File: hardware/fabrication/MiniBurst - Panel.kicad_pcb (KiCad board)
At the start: 2 copper layers, 30 x 128.5 mm, 9 parts

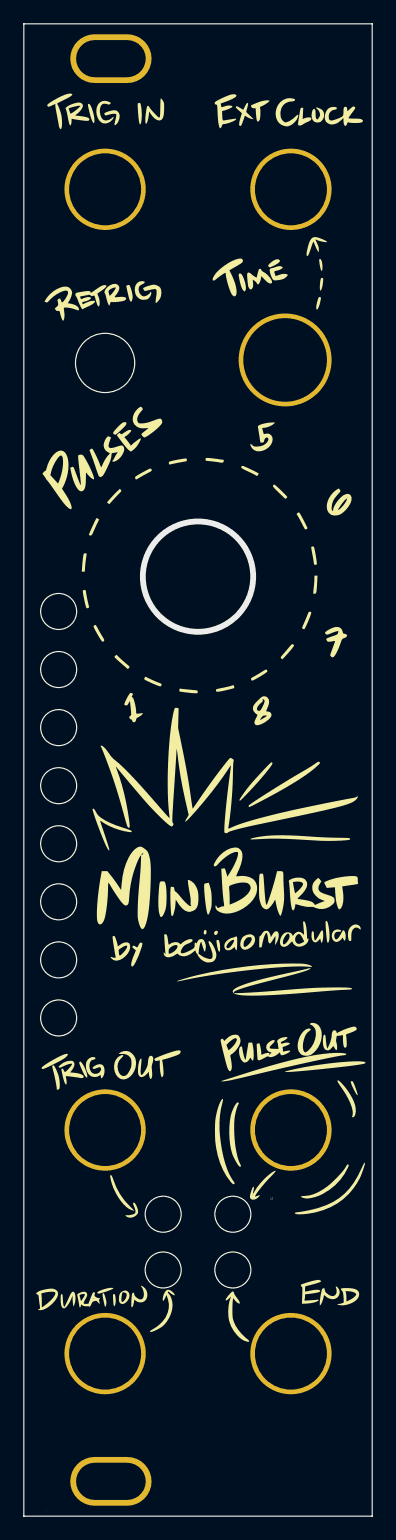
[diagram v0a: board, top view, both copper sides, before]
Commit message: Added copper fill to panel
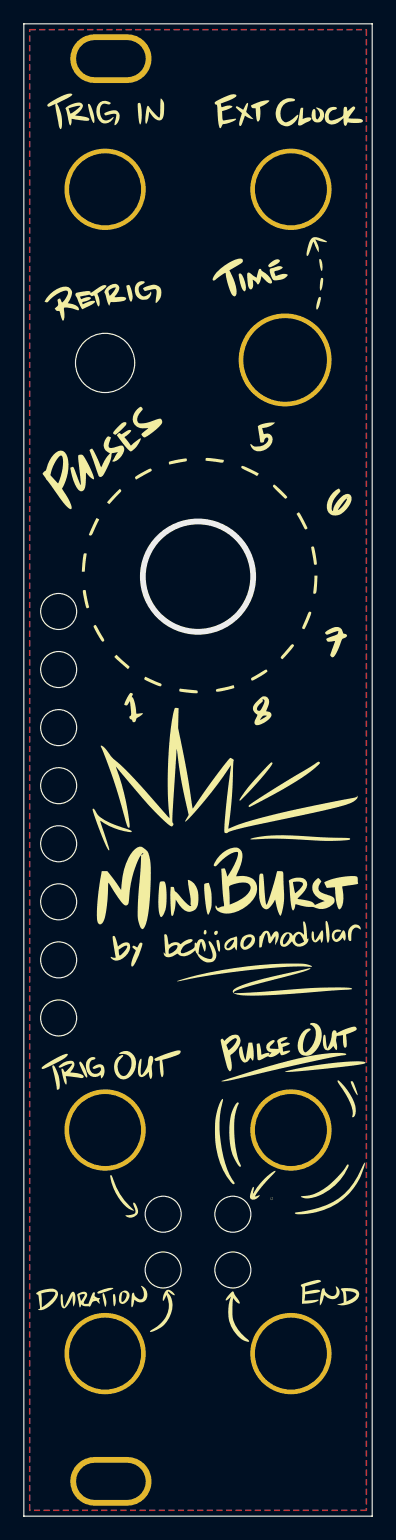
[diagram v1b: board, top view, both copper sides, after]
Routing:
- added copper zone on B.Cu, net (none)
- added copper zone on F.Cu, net (none)
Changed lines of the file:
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@@
 			(drillshape 0)
 			(scaleselection 1)
-			(outputdirectory "MiniBurst v0.1  - Front")
+			(outputdirectory "MiniBurst v0.1  - Panel")
 		)
 	)
@@
 		(net 0)
 	)
+	(zone
+		(net 0)
+		(net_name "")
+		(layer "F.Cu")
+		(hatch edge 0.5)
+		(connect_pads
+			(clearance 0.5)
+		)
+		(min_thickness 0.25)
+		(filled_areas_thickness no)
+		(fill yes
+			(thermal_gap 0.5)
+			(thermal_bridge_width 0.5)
+			(island_removal_mode 1)
+			(island_area_min 10)
+		)
+		(polygon
+			(pts
+				(xy 92.424 25.9) (xy 121.424 25.9) (xy 121.424 153.4) (xy 92.424 153.4)
+			)
+		)
+	)
+	(zone
+		(net 0)
+		(net_name "")
+		(layer "B.Cu")
+		(hatch edge 0.5)
+		(priority 1)
+		(connect_pads
+			(clearance 0.5)
+		)
+		(min_thickness 0.25)
+		(filled_areas_thickness no)
+		(fill yes
+			(thermal_gap 0.5)
+			(thermal_bridge_width 0.5)
+			(island_removal_mode 1)
+			(island_area_min 10)
+		)
+		(polygon
+			(pts
+				(xy 92.424 153.4) (xy 92.424 25.9) (xy 121.424 25.9) (xy 121.424 153.4)
+			)
+		)
+	)
 )
